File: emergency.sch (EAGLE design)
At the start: 33 parts, among them J1 8P8C, J6 MA02-2, Q2 BUZ11BH, U1 V23134J1052D642, U2 V23134J1052D642, U3 AP65111AWU-7, U4 TLP184

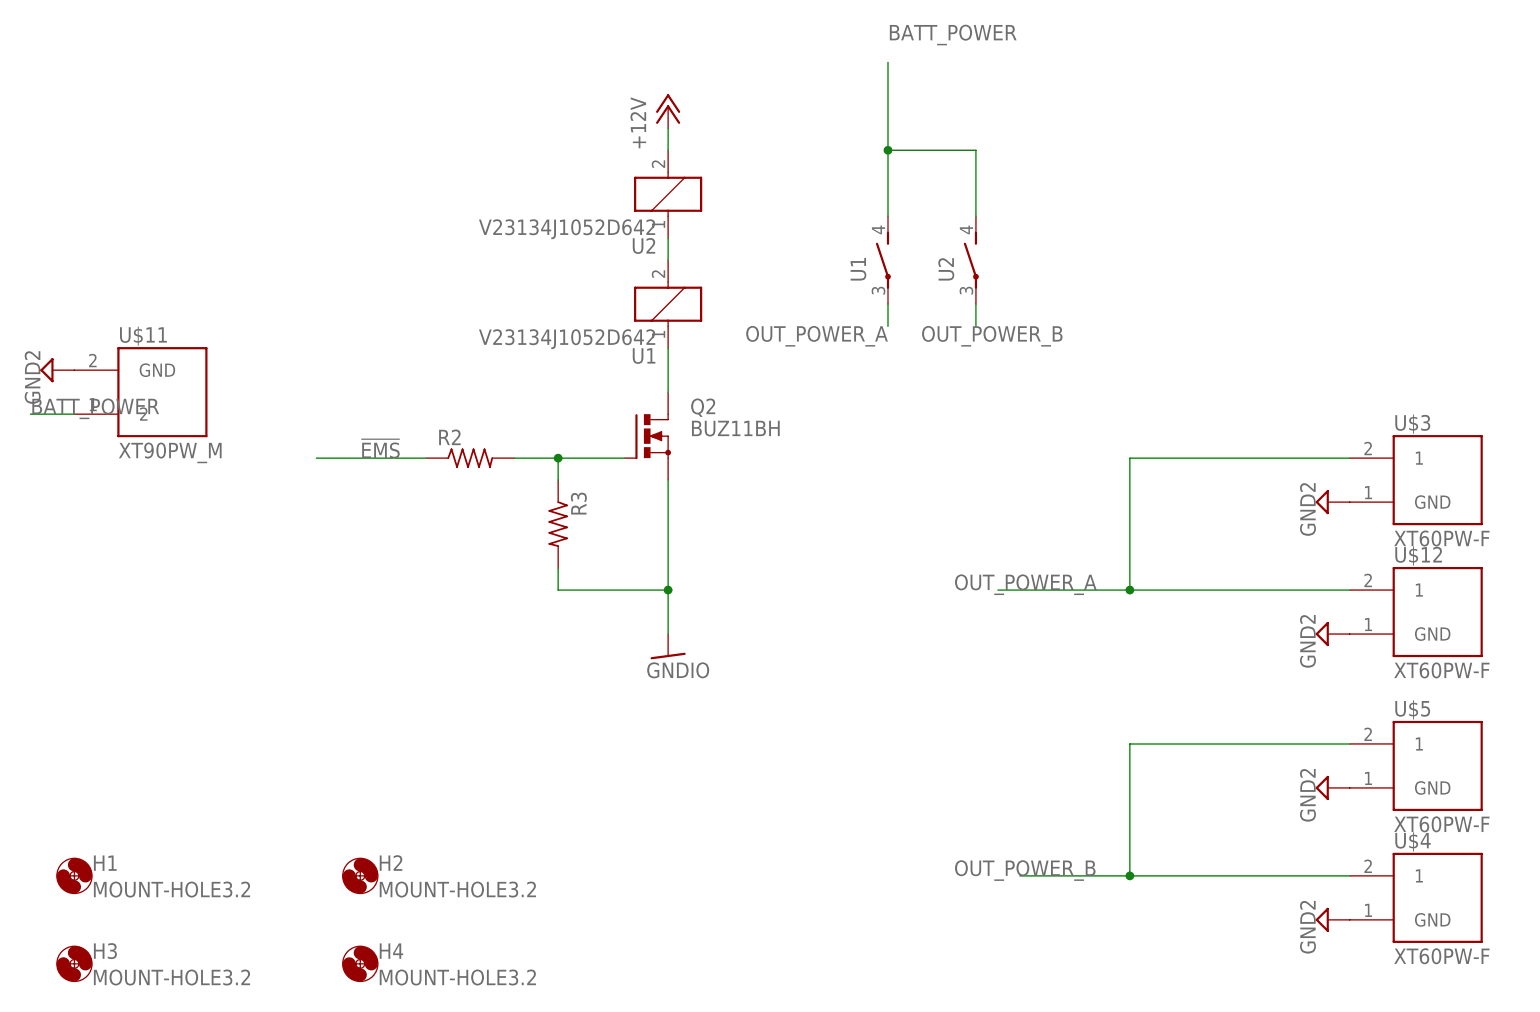
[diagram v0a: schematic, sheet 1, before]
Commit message: コイルの配線とベタの修正
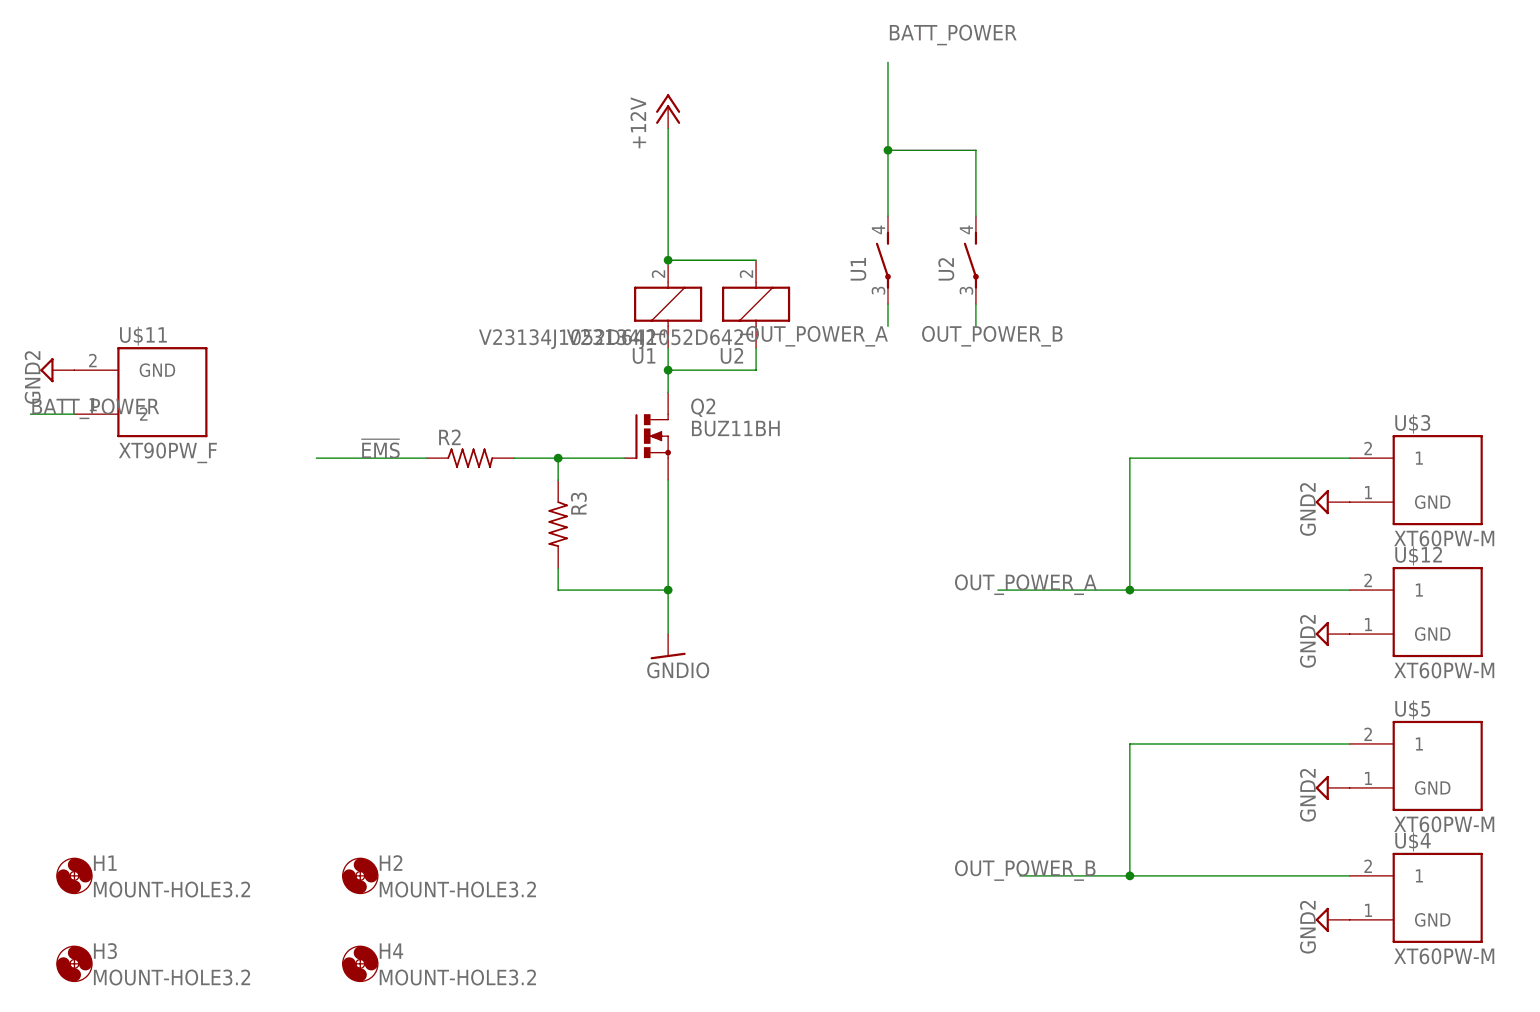
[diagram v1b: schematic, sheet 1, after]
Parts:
- U$11: value XT90PW_M -> XT90PW_F; device XT60_Connecotr:XT90PW_M -> XT60_Connecotr:XT90PW_F
- U$12, U$3, U$4, U$5: value XT60PW-F -> XT60PW-M; device XT60_Connecotr:XT60PW-F -> XT60_Connecotr:XT60PW-M
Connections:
- removed net N$4: U1A.2, U2A.1
- net +12V: now also U1A.2
- net N$6: now also U2A.1
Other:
- moved on the sheet: U2
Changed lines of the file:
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@@
 <part name="R3" library="rcl" library_urn="urn:adsk.eagle:library:334" deviceset="R-US_" device="R0603" package3d_urn="urn:adsk.eagle:package:23555/3"/>
 <part name="R2" library="rcl" library_urn="urn:adsk.eagle:library:334" deviceset="R-US_" device="R0603" package3d_urn="urn:adsk.eagle:package:23555/3"/>
-<part name="U$11" library="XT60_Connecotr" deviceset="XT90PW_M" device=""/>
+<part name="U$11" library="XT60_Connecotr" deviceset="XT90PW_F" device=""/>
 <part name="SUPPLY7" library="supply2" library_urn="urn:adsk.eagle:library:372" deviceset="GND2" device=""/>
-<part name="U$12" library="XT60_Connecotr" deviceset="XT60PW-F" device=""/>
+<part name="U$12" library="XT60_Connecotr" deviceset="XT60PW-M" device=""/>
 <part name="SUPPLY8" library="supply2" library_urn="urn:adsk.eagle:library:372" deviceset="GND2" device=""/>
 <part name="Q2" library="transistor-power" library_urn="urn:adsk.eagle:library:400" deviceset="BUZ11" device="BH" package3d_urn="urn:adsk.eagle:package:29490/1"/>
@@
 <part name="+3V1" library="supply1" library_urn="urn:adsk.eagle:library:371" deviceset="+3V3" device=""/>
 <part name="R5" library="rcl" library_urn="urn:adsk.eagle:library:334" deviceset="R-US_" device="R0603" package3d_urn="urn:adsk.eagle:package:23555/3" value="47k"/>
-<part name="U$3" library="XT60_Connecotr" deviceset="XT60PW-F" device=""/>
+<part name="U$3" library="XT60_Connecotr" deviceset="XT60PW-M" device=""/>
 <part name="SUPPLY1" library="supply2" library_urn="urn:adsk.eagle:library:372" deviceset="GND2" device=""/>
 <part name="P+3" library="supply1" library_urn="urn:adsk.eagle:library:371" deviceset="+12V" device=""/>
 <part name="U2" library="relay" deviceset="V23134J1052D642" device=""/>
-<part name="U$4" library="XT60_Connecotr" deviceset="XT60PW-F" device=""/>
+<part name="U$4" library="XT60_Connecotr" deviceset="XT60PW-M" device=""/>
 <part name="SUPPLY2" library="supply2" library_urn="urn:adsk.eagle:library:372" deviceset="GND2" device=""/>
-<part name="U$5" library="XT60_Connecotr" deviceset="XT60PW-F" device=""/>
+<part name="U$5" library="XT60_Connecotr" deviceset="XT60PW-M" device=""/>
 <part name="SUPPLY3" library="supply2" library_urn="urn:adsk.eagle:library:372" deviceset="GND2" device=""/>
 <part name="GND6" library="supply1" library_urn="urn:adsk.eagle:library:371" deviceset="GNDIO" device=""/>
@@
 <attribute name="VALUE" x="146.685" y="65.913" size="1.778" layer="96" rot="R270"/>
 </instance>
-<instance part="U2" gate="A" x="73.66" y="99.06" smashed="yes" rot="R180">
-<attribute name="VALUE" x="72.39" y="96.139" size="1.778" layer="96" rot="R180"/>
-<attribute name="PART" x="72.39" y="93.98" size="1.778" layer="95" rot="R180"/>
+<instance part="U2" gate="A" x="83.82" y="86.36" smashed="yes" rot="R180">
+<attribute name="VALUE" x="82.55" y="83.439" size="1.778" layer="96" rot="R180"/>
+<attribute name="PART" x="82.55" y="81.28" size="1.778" layer="95" rot="R180"/>
 </instance>
 <instance part="U2" gate="B" x="109.22" y="91.44" smashed="yes">
@@
 </segment>
 </net>
-<net name="+12V" class="0">
-<segment>
-<pinref part="P+2" gate="1" pin="+12V"/>
-<pinref part="U2" gate="A" pin="2"/>
-<wire x1="73.66" y1="106.68" x2="73.66" y2="104.14" width="0.1524" layer="91"/>
-</segment>
-</net>
-<net name="N$4" class="0">
-<segment>
-<pinref part="U2" gate="A" pin="1"/>
-<pinref part="U1" gate="A" pin="2"/>
-<wire x1="73.66" y1="91.44" x2="73.66" y2="93.98" width="0.1524" layer="91"/>
-</segment>
-</net>
 <net name="N$6" class="0">
 <segment>
 <pinref part="Q2" gate="1" pin="D"/>
 <pinref part="U1" gate="A" pin="1"/>
-<wire x1="73.66" y1="81.28" x2="73.66" y2="76.2" width="0.1524" layer="91"/>
+<wire x1="73.66" y1="81.28" x2="73.66" y2="78.74" width="0.1524" layer="91"/>
+<pinref part="U2" gate="A" pin="1"/>
+<wire x1="73.66" y1="78.74" x2="73.66" y2="76.2" width="0.1524" layer="91"/>
+<wire x1="73.66" y1="78.74" x2="83.82" y2="78.74" width="0.1524" layer="91"/>
+<wire x1="83.82" y1="78.74" x2="83.82" y2="81.28" width="0.1524" layer="91"/>
+<junction x="73.66" y="78.74"/>
 </segment>
 </net>
@@
 </segment>
 </net>
+<net name="+12V" class="0">
+<segment>
+<pinref part="U2" gate="A" pin="2"/>
+<pinref part="U1" gate="A" pin="2"/>
+<wire x1="83.82" y1="91.44" x2="73.66" y2="91.44" width="0.1524" layer="91"/>
+<pinref part="P+2" gate="1" pin="+12V"/>
+<wire x1="73.66" y1="91.44" x2="73.66" y2="106.68" width="0.1524" layer="91"/>
+<junction x="73.66" y="91.44"/>
+</segment>
+</net>

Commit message: リレーのライブラリの修正
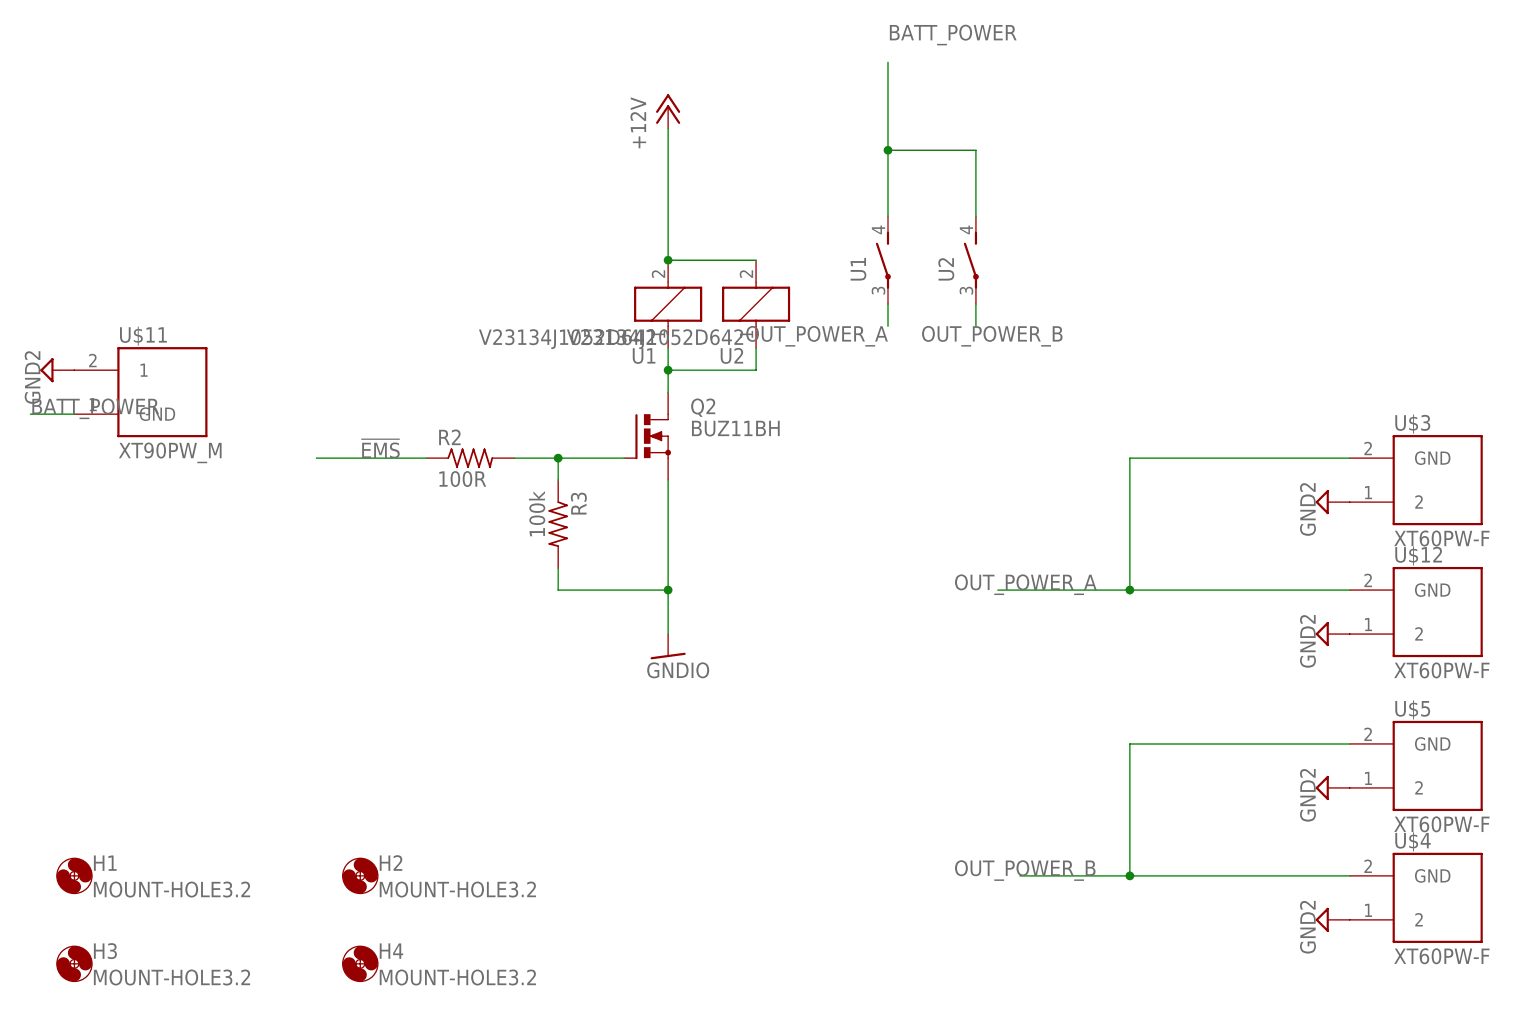
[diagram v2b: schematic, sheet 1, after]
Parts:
- R2: value (none) -> 100R
- R3: value (none) -> 100k
- U$11: value XT90PW_F -> XT90PW_M; device XT60_Connecotr:XT90PW_F -> XT60_Connecotr:XT90PW_M
- U$12, U$3, U$4, U$5: value XT60PW-M -> XT60PW-F; device XT60_Connecotr:XT60PW-M -> XT60_Connecotr:XT60PW-F
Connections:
- net BATT_POWER: now also U$11.GND; no longer U$11.2
- net GND2: now also U$11.1, U$12.2, U$3.2, U$4.2, U$5.2; no longer U$11.GND, U$12.GND, U$3.GND, U$4.GND, U$5.GND
- net OUT_POWER_A: now also U$12.GND, U$3.GND; no longer U$12.1, U$3.1
- net OUT_POWER_B: now also U$4.GND, U$5.GND; no longer U$4.1, U$5.1
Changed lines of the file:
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@@
 </classes>
 <parts>
-<part name="R3" library="rcl" library_urn="urn:adsk.eagle:library:334" deviceset="R-US_" device="R0603" package3d_urn="urn:adsk.eagle:package:23555/3"/>
-<part name="R2" library="rcl" library_urn="urn:adsk.eagle:library:334" deviceset="R-US_" device="R0603" package3d_urn="urn:adsk.eagle:package:23555/3"/>
-<part name="U$11" library="XT60_Connecotr" deviceset="XT90PW_F" device=""/>
+<part name="R3" library="rcl" library_urn="urn:adsk.eagle:library:334" deviceset="R-US_" device="R0603" package3d_urn="urn:adsk.eagle:package:23555/3" value="100k"/>
+<part name="R2" library="rcl" library_urn="urn:adsk.eagle:library:334" deviceset="R-US_" device="R0603" package3d_urn="urn:adsk.eagle:package:23555/3" value="100R"/>
+<part name="U$11" library="XT60_Connecotr" deviceset="XT90PW_M" device=""/>
 <part name="SUPPLY7" library="supply2" library_urn="urn:adsk.eagle:library:372" deviceset="GND2" device=""/>
-<part name="U$12" library="XT60_Connecotr" deviceset="XT60PW-M" device=""/>
+<part name="U$12" library="XT60_Connecotr" deviceset="XT60PW-F" device=""/>
 <part name="SUPPLY8" library="supply2" library_urn="urn:adsk.eagle:library:372" deviceset="GND2" device=""/>
 <part name="Q2" library="transistor-power" library_urn="urn:adsk.eagle:library:400" deviceset="BUZ11" device="BH" package3d_urn="urn:adsk.eagle:package:29490/1"/>
@@
 <part name="+3V1" library="supply1" library_urn="urn:adsk.eagle:library:371" deviceset="+3V3" device=""/>
 <part name="R5" library="rcl" library_urn="urn:adsk.eagle:library:334" deviceset="R-US_" device="R0603" package3d_urn="urn:adsk.eagle:package:23555/3" value="47k"/>
-<part name="U$3" library="XT60_Connecotr" deviceset="XT60PW-M" device=""/>
+<part name="U$3" library="XT60_Connecotr" deviceset="XT60PW-F" device=""/>
 <part name="SUPPLY1" library="supply2" library_urn="urn:adsk.eagle:library:372" deviceset="GND2" device=""/>
 <part name="P+3" library="supply1" library_urn="urn:adsk.eagle:library:371" deviceset="+12V" device=""/>
 <part name="U2" library="relay" deviceset="V23134J1052D642" device=""/>
-<part name="U$4" library="XT60_Connecotr" deviceset="XT60PW-M" device=""/>
+<part name="U$4" library="XT60_Connecotr" deviceset="XT60PW-F" device=""/>
 <part name="SUPPLY2" library="supply2" library_urn="urn:adsk.eagle:library:372" deviceset="GND2" device=""/>
-<part name="U$5" library="XT60_Connecotr" deviceset="XT60PW-M" device=""/>
+<part name="U$5" library="XT60_Connecotr" deviceset="XT60PW-F" device=""/>
 <part name="SUPPLY3" library="supply2" library_urn="urn:adsk.eagle:library:372" deviceset="GND2" device=""/>
 <part name="GND6" library="supply1" library_urn="urn:adsk.eagle:library:371" deviceset="GNDIO" device=""/>
@@
 <net name="GND2" class="0">
 <segment>
-<pinref part="U$11" gate="G$1" pin="GND"/>
+<pinref part="U$11" gate="G$1" pin="1"/>
 <pinref part="SUPPLY7" gate="G$1" pin="GND2"/>
 </segment>
 <segment>
-<pinref part="U$12" gate="G$1" pin="GND"/>
+<pinref part="U$12" gate="G$1" pin="2"/>
 <pinref part="SUPPLY8" gate="G$1" pin="GND2"/>
 </segment>
 <segment>
-<pinref part="U$3" gate="G$1" pin="GND"/>
+<pinref part="U$3" gate="G$1" pin="2"/>
 <pinref part="SUPPLY1" gate="G$1" pin="GND2"/>
 </segment>
 <segment>
-<pinref part="U$4" gate="G$1" pin="GND"/>
+<pinref part="U$4" gate="G$1" pin="2"/>
 <pinref part="SUPPLY2" gate="G$1" pin="GND2"/>
 </segment>
 <segment>
-<pinref part="U$5" gate="G$1" pin="GND"/>
+<pinref part="U$5" gate="G$1" pin="2"/>
 <pinref part="SUPPLY3" gate="G$1" pin="GND2"/>
 </segment>
@@
 </segment>
 <segment>
-<pinref part="U$11" gate="G$1" pin="2"/>
+<pinref part="U$11" gate="G$1" pin="GND"/>
 <wire x1="5.08" y1="73.66" x2="0" y2="73.66" width="0.1524" layer="91"/>
 <label x="0" y="73.66" size="1.778" layer="95"/>
@@
 </segment>
 <segment>
-<pinref part="U$5" gate="G$1" pin="1"/>
+<pinref part="U$5" gate="G$1" pin="GND"/>
 <wire x1="152.4" y1="35.56" x2="127" y2="35.56" width="0.1524" layer="91"/>
 <wire x1="127" y1="35.56" x2="127" y2="20.32" width="0.1524" layer="91"/>
-<pinref part="U$4" gate="G$1" pin="1"/>
+<pinref part="U$4" gate="G$1" pin="GND"/>
 <wire x1="127" y1="20.32" x2="152.4" y2="20.32" width="0.1524" layer="91"/>
 <wire x1="127" y1="20.32" x2="114.3" y2="20.32" width="0.1524" layer="91"/>
@@
 <net name="OUT_POWER_A" class="0">
 <segment>
-<pinref part="U$3" gate="G$1" pin="1"/>
+<pinref part="U$3" gate="G$1" pin="GND"/>
 <wire x1="152.4" y1="68.58" x2="127" y2="68.58" width="0.1524" layer="91"/>
 <wire x1="127" y1="68.58" x2="127" y2="53.34" width="0.1524" layer="91"/>
-<pinref part="U$12" gate="G$1" pin="1"/>
+<pinref part="U$12" gate="G$1" pin="GND"/>
 <wire x1="127" y1="53.34" x2="152.4" y2="53.34" width="0.1524" layer="91"/>
 <wire x1="127" y1="53.34" x2="111.76" y2="53.34" width="0.1524" layer="91"/>
